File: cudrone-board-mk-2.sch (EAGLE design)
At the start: 40 parts, among them Q1 BSS138, U1 EDISON_CONNECTOR_FULLMOUNTING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, U2 FTS31XS-U, U4 TPS62065

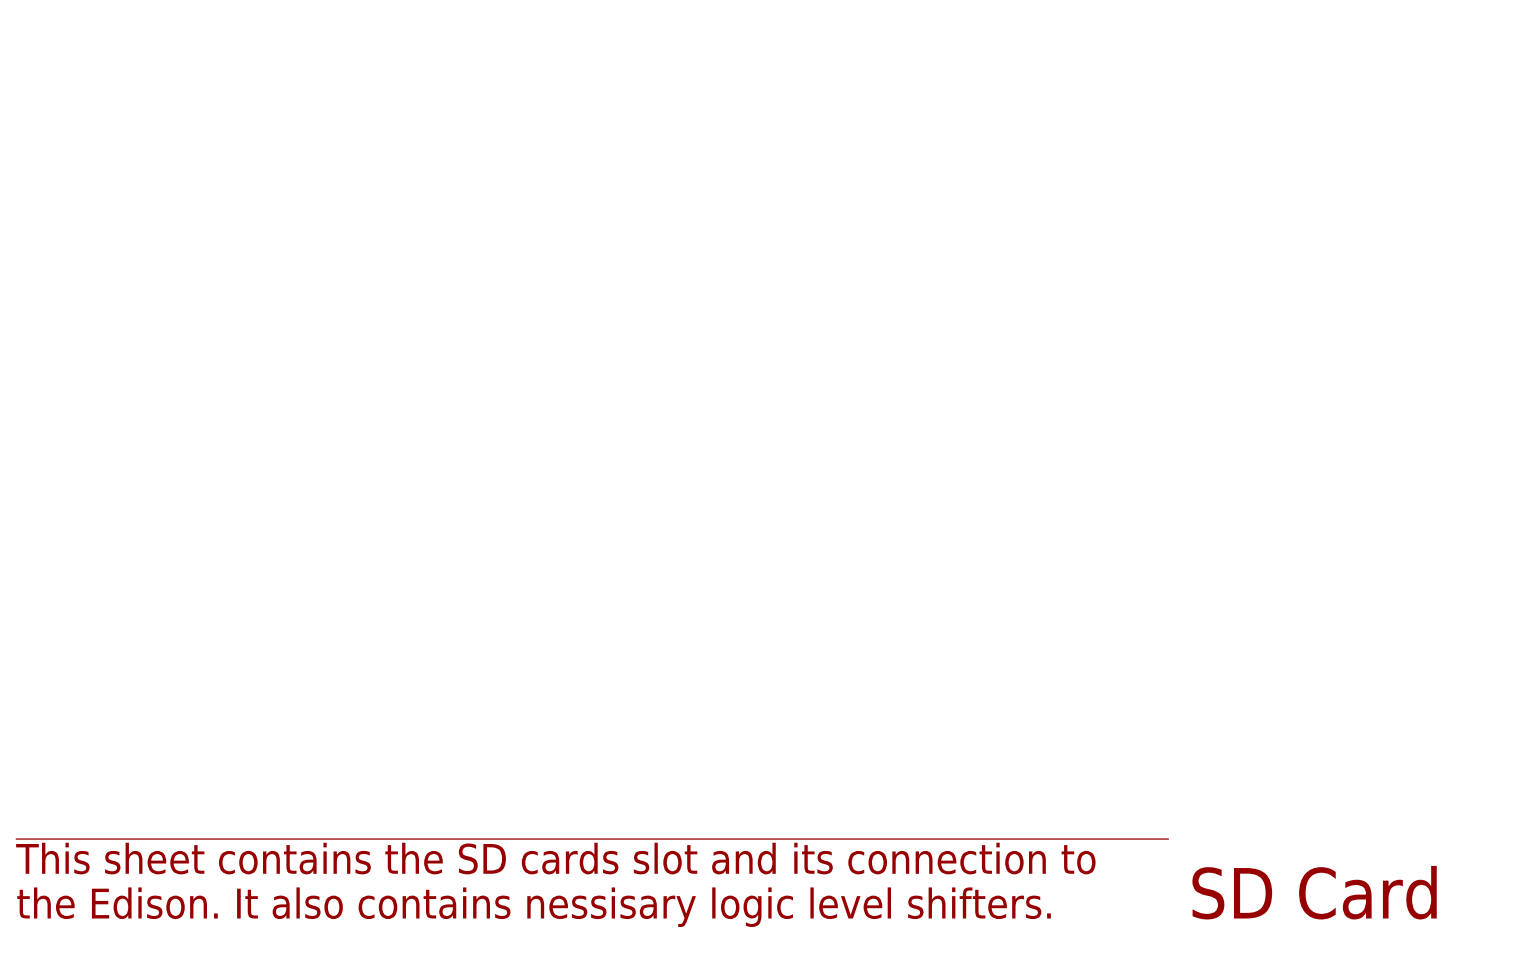
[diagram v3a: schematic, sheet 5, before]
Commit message: Added sd card
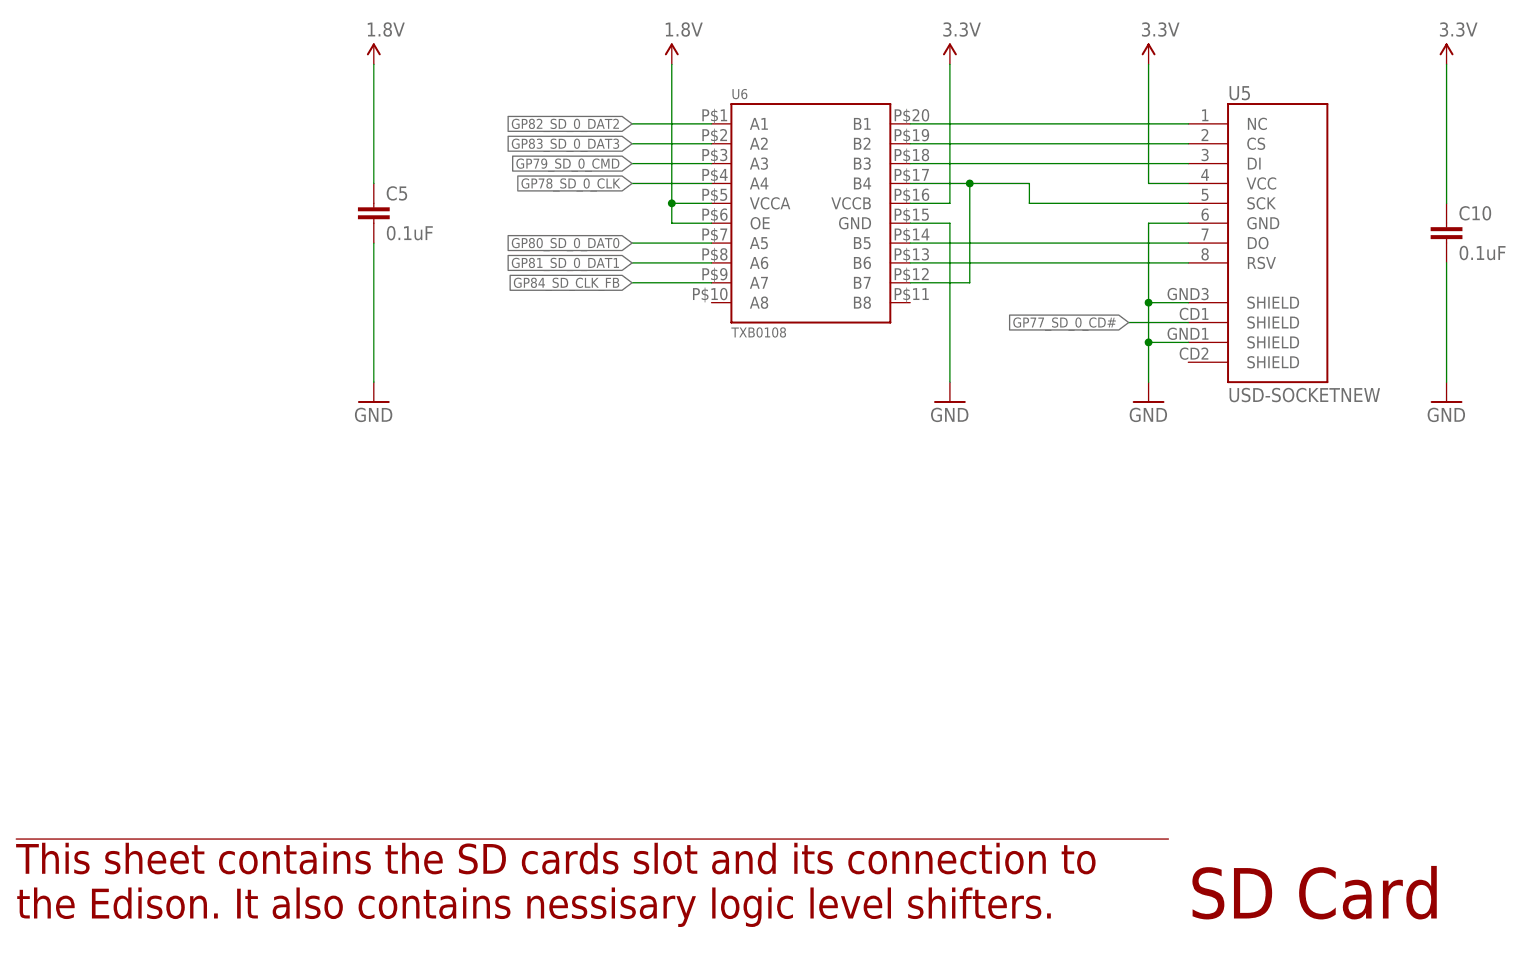
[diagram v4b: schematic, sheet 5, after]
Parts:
- added C10, C5: 0.1uF, SparkFun-Capacitors:0.1UF-25V(+80/-20%)(0603)
- added U5: USD-SOCKETNEW, SparkFun-Connectors:USD-SOCKETNEW
- added U6: TXB0108, Testing:TXB0108
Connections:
- new net N$20: U5.NC, U6.B1
- new net N$21: U5.CS, U6.B2
- new net N$22: U5.DI, U6.B3
- new net N$23: U5.DO, U6.B5
- new net N$24: U5.RSV, U6.B6
- new net SCK: U5.SCK, U6.B4, U6.B7
- net 1.8V: now also C5.1, U6.OE, U6.VCCA
- net 3.3V: now also C10.1, U5.VCC, U6.VCCB
- net GND: now also C10.2, C5.2, U5.GND, U5.SHIELD@1, U5.SHIELD@3, U6.GND
- net GP77_SD_0_CD#: now also U5.SHIELD@2
- net GP78_SD_0_CLK: now also U6.A4
- net GP79_SD_0_CMD: now also U6.A3
- net GP80_SD_0_DAT0: now also U6.A5
- net GP81_SD_0_DAT1: now also U6.A6
- net GP82_SD_0_DAT2: now also U6.A1
- net GP83_SD_0_DAT3: now also U6.A2
- net GP84_SD_CLK_FB: now also U6.A7
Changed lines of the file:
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@@
 <part name="R12" library="SparkFun-Resistors" deviceset="100KOHM1/10W1%(0603)" device="" value="100k"/>
 <part name="GND20" library="SparkFun-Aesthetics" deviceset="GND" device=""/>
+<part name="U5" library="SparkFun-Connectors" deviceset="USD-SOCKET" device="NEW"/>
+<part name="GND13" library="SparkFun-Aesthetics" deviceset="GND" device=""/>
+<part name="U6" library="Testing" deviceset="TXB0108" device=""/>
+<part name="GND23" library="SparkFun-Aesthetics" deviceset="GND" device=""/>
+<part name="SUPPLY12" library="SparkFun-Aesthetics" deviceset="3.3V" device=""/>
+<part name="SUPPLY13" library="SparkFun-Aesthetics" deviceset="3.3V" device=""/>
+<part name="SUPPLY14" library="SparkFun-Aesthetics" deviceset="1.8V" device=""/>
+<part name="C5" library="SparkFun-Capacitors" deviceset="0.1UF-25V(+80/-20%)(0603)" device="" value="0.1uF"/>
+<part name="C10" library="SparkFun-Capacitors" deviceset="0.1UF-25V(+80/-20%)(0603)" device="" value="0.1uF"/>
+<part name="SUPPLY15" library="SparkFun-Aesthetics" deviceset="1.8V" device=""/>
+<part name="GND24" library="SparkFun-Aesthetics" deviceset="GND" device=""/>
+<part name="GND25" library="SparkFun-Aesthetics" deviceset="GND" device=""/>
+<part name="SUPPLY16" library="SparkFun-Aesthetics" deviceset="3.3V" device=""/>
 </parts>
 <sheets>
@@
 <instance part="FRAME5" gate="G$1" x="0" y="0"/>
 <instance part="FRAME5" gate="G$2" x="147.32" y="0"/>
+<instance part="U5" gate="G$1" x="157.48" y="114.3"/>
+<instance part="GND13" gate="1" x="144.78" y="91.44"/>
+<instance part="U6" gate="G$1" x="109.22" y="116.84"/>
+<instance part="GND23" gate="1" x="119.38" y="91.44"/>
+<instance part="SUPPLY12" gate="G$1" x="119.38" y="134.62"/>
+<instance part="SUPPLY13" gate="G$1" x="144.78" y="134.62"/>
+<instance part="SUPPLY14" gate="G$1" x="83.82" y="134.62"/>
+<instance part="C5" gate="G$1" x="45.72" y="114.3"/>
+<instance part="C10" gate="G$1" x="182.88" y="111.76"/>
+<instance part="SUPPLY15" gate="G$1" x="45.72" y="134.62"/>
+<instance part="GND24" gate="1" x="45.72" y="91.44"/>
+<instance part="GND25" gate="1" x="182.88" y="91.44"/>
+<instance part="SUPPLY16" gate="G$1" x="182.88" y="134.62"/>
 </instances>
 <busses>
 </busses>
 <nets>
+<net name="GND" class="0">
+<segment>
+<pinref part="U5" gate="G$1" pin="SHIELD@1"/>
+<wire x1="149.86" y1="104.14" x2="144.78" y2="104.14" width="0.1524" layer="91"/>
+<wire x1="144.78" y1="104.14" x2="144.78" y2="99.06" width="0.1524" layer="91"/>
+<pinref part="U5" gate="G$1" pin="SHIELD@3"/>
+<wire x1="149.86" y1="99.06" x2="144.78" y2="99.06" width="0.1524" layer="91"/>
+<junction x="144.78" y="99.06"/>
+<pinref part="GND13" gate="1" pin="GND"/>
+<wire x1="144.78" y1="93.98" x2="144.78" y2="99.06" width="0.1524" layer="91"/>
+<pinref part="U5" gate="G$1" pin="GND"/>
+<wire x1="149.86" y1="114.3" x2="144.78" y2="114.3" width="0.1524" layer="91"/>
+<wire x1="144.78" y1="114.3" x2="144.78" y2="104.14" width="0.1524" layer="91"/>
+<junction x="144.78" y="104.14"/>
+</segment>
+<segment>
+<pinref part="U6" gate="G$1" pin="GND"/>
+<wire x1="114.3" y1="114.3" x2="119.38" y2="114.3" width="0.1524" layer="91"/>
+<wire x1="119.38" y1="114.3" x2="119.38" y2="93.98" width="0.1524" layer="91"/>
+<pinref part="GND23" gate="1" pin="GND"/>
+</segment>
+<segment>
+<pinref part="C5" gate="G$1" pin="2"/>
+<pinref part="GND24" gate="1" pin="GND"/>
+<wire x1="45.72" y1="93.98" x2="45.72" y2="111.76" width="0.1524" layer="91"/>
+</segment>
+<segment>
+<pinref part="C10" gate="G$1" pin="2"/>
+<pinref part="GND25" gate="1" pin="GND"/>
+<wire x1="182.88" y1="93.98" x2="182.88" y2="109.22" width="0.1524" layer="91"/>
+</segment>
+</net>
+<net name="GP78_SD_0_CLK" class="0">
+<segment>
+<wire x1="88.9" y1="119.38" x2="78.74" y2="119.38" width="0.1524" layer="91"/>
+<label x="78.74" y="119.38" size="1.27" layer="95" rot="R180" xref="yes"/>
+<pinref part="U6" gate="G$1" pin="A4"/>
+</segment>
+</net>
+<net name="GP77_SD_0_CD#" class="0">
+<segment>
+<wire x1="149.86" y1="101.6" x2="142.24" y2="101.6" width="0.1524" layer="91"/>
+<label x="142.24" y="101.6" size="1.27" layer="95" rot="R180" xref="yes"/>
+<pinref part="U5" gate="G$1" pin="SHIELD@2"/>
+</segment>
+</net>
+<net name="GP79_SD_0_CMD" class="0">
+<segment>
+<wire x1="88.9" y1="121.92" x2="78.74" y2="121.92" width="0.1524" layer="91"/>
+<label x="78.74" y="121.92" size="1.27" layer="95" rot="R180" xref="yes"/>
+<pinref part="U6" gate="G$1" pin="A3"/>
+</segment>
+</net>
+<net name="GP80_SD_0_DAT0" class="0">
+<segment>
+<wire x1="88.9" y1="111.76" x2="78.74" y2="111.76" width="0.1524" layer="91"/>
+<label x="78.74" y="111.76" size="1.27" layer="95" rot="R180" xref="yes"/>
+<pinref part="U6" gate="G$1" pin="A5"/>
+</segment>
+</net>
+<net name="GP81_SD_0_DAT1" class="0">
+<segment>
+<wire x1="88.9" y1="109.22" x2="78.74" y2="109.22" width="0.1524" layer="91"/>
+<label x="78.74" y="109.22" size="1.27" layer="95" rot="R180" xref="yes"/>
+<pinref part="U6" gate="G$1" pin="A6"/>
+</segment>
+</net>
+<net name="GP82_SD_0_DAT2" class="0">
+<segment>
+<wire x1="88.9" y1="127" x2="78.74" y2="127" width="0.1524" layer="91"/>
+<label x="78.74" y="127" size="1.27" layer="95" rot="R180" xref="yes"/>
+<pinref part="U6" gate="G$1" pin="A1"/>
+</segment>
+</net>
+<net name="GP83_SD_0_DAT3" class="0">
+<segment>
+<wire x1="88.9" y1="124.46" x2="78.74" y2="124.46" width="0.1524" layer="91"/>
+<label x="78.74" y="124.46" size="1.27" layer="95" rot="R180" xref="yes"/>
+<pinref part="U6" gate="G$1" pin="A2"/>
+</segment>
+</net>
+<net name="N$20" class="0">
+<segment>
+<pinref part="U6" gate="G$1" pin="B1"/>
+<pinref part="U5" gate="G$1" pin="NC"/>
+<wire x1="114.3" y1="127" x2="149.86" y2="127" width="0.1524" layer="91"/>
+</segment>
+</net>
+<net name="N$21" class="0">
+<segment>
+<pinref part="U5" gate="G$1" pin="CS"/>
+<pinref part="U6" gate="G$1" pin="B2"/>
+<wire x1="149.86" y1="124.46" x2="114.3" y2="124.46" width="0.1524" layer="91"/>
+</segment>
+</net>
+<net name="N$22" class="0">
+<segment>
+<pinref part="U6" gate="G$1" pin="B3"/>
+<pinref part="U5" gate="G$1" pin="DI"/>
+<wire x1="114.3" y1="121.92" x2="149.86" y2="121.92" width="0.1524" layer="91"/>
+</segment>
+</net>
+<net name="SCK" class="0">
+<segment>
+<pinref part="U6" gate="G$1" pin="B4"/>
+<wire x1="114.3" y1="119.38" x2="121.92" y2="119.38" width="0.1524" layer="91"/>
+<wire x1="121.92" y1="119.38" x2="129.54" y2="119.38" width="0.1524" layer="91"/>
+<wire x1="129.54" y1="119.38" x2="129.54" y2="116.84" width="0.1524" layer="91"/>
+<pinref part="U5" gate="G$1" pin="SCK"/>
+<wire x1="129.54" y1="116.84" x2="149.86" y2="116.84" width="0.1524" layer="91"/>
+<pinref part="U6" gate="G$1" pin="B7"/>
+<wire x1="114.3" y1="106.68" x2="121.92" y2="106.68" width="0.1524" layer="91"/>
+<wire x1="121.92" y1="106.68" x2="121.92" y2="119.38" width="0.1524" layer="91"/>
+<junction x="121.92" y="119.38"/>
+</segment>
+</net>
+<net name="N$23" class="0">
+<segment>
+<pinref part="U6" gate="G$1" pin="B5"/>
+<pinref part="U5" gate="G$1" pin="DO"/>
+<wire x1="114.3" y1="111.76" x2="149.86" y2="111.76" width="0.1524" layer="91"/>
+</segment>
+</net>
+<net name="N$24" class="0">
+<segment>
+<pinref part="U6" gate="G$1" pin="B6"/>
+<pinref part="U5" gate="G$1" pin="RSV"/>
+<wire x1="114.3" y1="109.22" x2="149.86" y2="109.22" width="0.1524" layer="91"/>
+</segment>
+</net>
+<net name="3.3V" class="0">
+<segment>
+<pinref part="U6" gate="G$1" pin="VCCB"/>
+<wire x1="114.3" y1="116.84" x2="119.38" y2="116.84" width="0.1524" layer="91"/>
+<wire x1="119.38" y1="116.84" x2="119.38" y2="134.62" width="0.1524" layer="91"/>
+<pinref part="SUPPLY12" gate="G$1" pin="3.3V"/>
+</segment>
+<segment>
+<pinref part="U5" gate="G$1" pin="VCC"/>
+<wire x1="149.86" y1="119.38" x2="144.78" y2="119.38" width="0.1524" layer="91"/>
+<wire x1="144.78" y1="119.38" x2="144.78" y2="134.62" width="0.1524" layer="91"/>
+<pinref part="SUPPLY13" gate="G$1" pin="3.3V"/>
+</segment>
+<segment>
+<pinref part="C10" gate="G$1" pin="1"/>
+<pinref part="SUPPLY16" gate="G$1" pin="3.3V"/>
+<wire x1="182.88" y1="134.62" x2="182.88" y2="116.84" width="0.1524" layer="91"/>
+</segment>
+</net>
+<net name="1.8V" class="0">
+<segment>
+<pinref part="U6" gate="G$1" pin="VCCA"/>
+<pinref part="SUPPLY14" gate="G$1" pin="1.8V"/>
+<wire x1="88.9" y1="116.84" x2="83.82" y2="116.84" width="0.1524" layer="91"/>
+<wire x1="83.82" y1="116.84" x2="83.82" y2="134.62" width="0.1524" layer="91"/>
+<pinref part="U6" gate="G$1" pin="OE"/>
+<wire x1="88.9" y1="114.3" x2="83.82" y2="114.3" width="0.1524" layer="91"/>
+<wire x1="83.82" y1="114.3" x2="83.82" y2="116.84" width="0.1524" layer="91"/>
+<junction x="83.82" y="116.84"/>
+</segment>
+<segment>
+<pinref part="C5" gate="G$1" pin="1"/>
+<pinref part="SUPPLY15" gate="G$1" pin="1.8V"/>
+<wire x1="45.72" y1="134.62" x2="45.72" y2="119.38" width="0.1524" layer="91"/>
+</segment>
+</net>
+<net name="GP84_SD_CLK_FB" class="0">
+<segment>
+<wire x1="88.9" y1="106.68" x2="78.74" y2="106.68" width="0.1524" layer="91"/>
+<label x="78.74" y="106.68" size="1.27" layer="95" rot="R180" xref="yes"/>
+<pinref part="U6" gate="G$1" pin="A7"/>
+</segment>
+</net>
 </nets>
 </sheet>
